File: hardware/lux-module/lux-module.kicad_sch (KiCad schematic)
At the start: 7 parts, among them J1 Conn_01x04, U1 TSL25911FN, U2 TPD3E001DRLR

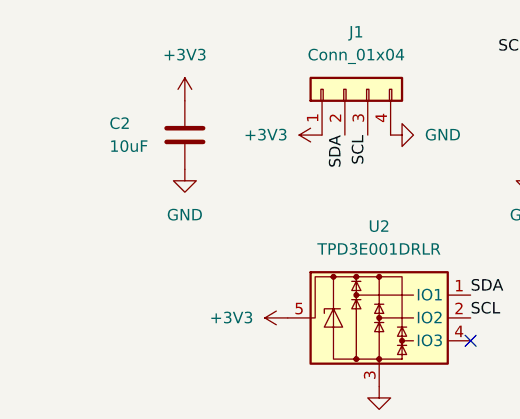
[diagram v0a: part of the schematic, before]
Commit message: review, add vias & ground pour
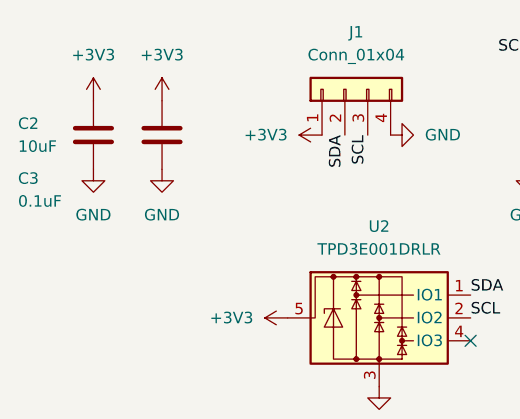
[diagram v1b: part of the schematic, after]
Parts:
- added C3: 0.1uF, Capacitor_SMD:C_0603_1608Metric, symbol Device:C
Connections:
- net +3V3: now also C3.1
- net GND: now also C3.2
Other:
- moved on the sheet: C2

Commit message: pad clearance & BOM fixes
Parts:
- C3: MPN GRM155R71H104KE14D -> CC0603KRX7R9BB104
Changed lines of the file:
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@@
 			)
 		)
-		(property "MPN" "GRM155R71H104KE14D"
+		(property "MPN" "CC0603KRX7R9BB104"
 			(at 82.55 96.52 0)
 			(effects

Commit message: swap connector in progress
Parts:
- J1: footprint 530480410:MOLEX_530480410 -> S04B_PASK_2:CONN4_S04B-PASK_JST
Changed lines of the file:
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@@
 			)
 		)
-		(property "Footprint" "530480410:MOLEX_530480410"
+		(property "Footprint" "S04B_PASK_2:CONN4_S04B-PASK_JST"
 			(at 102.87 91.44 0)
 			(effects

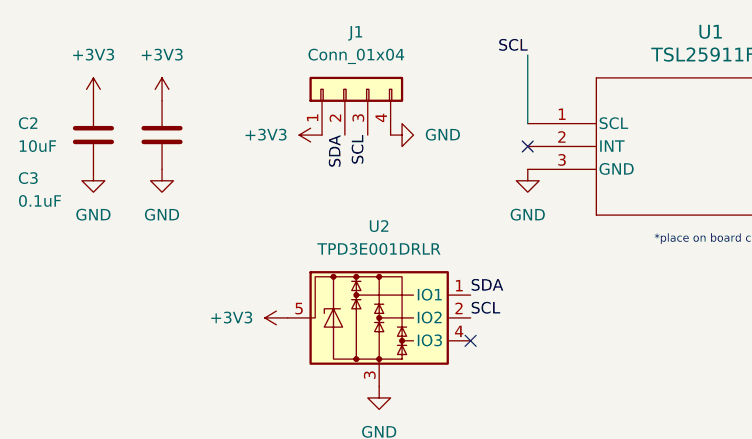
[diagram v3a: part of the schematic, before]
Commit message: connector fixes
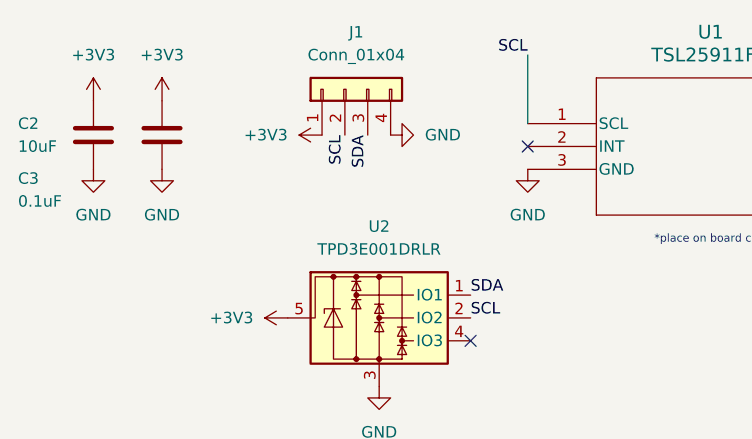
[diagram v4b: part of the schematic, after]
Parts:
- J1: MPN N/A -> S04B-PASK-2; Purchase No -> Yes
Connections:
- net SCL: now also J1.2 (Pin_2); no longer J1.3 (Pin_3)
- net SDA: now also J1.3 (Pin_3); no longer J1.2 (Pin_2)
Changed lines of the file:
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@@
 	)
 	(label "SDA"
-		(at 102.87 96.52 270)
+		(at 163.83 87.63 0)
 		(fields_autoplaced yes)
 		(effects
@@
 				(size 1.27 1.27)
 			)
-			(justify right bottom)
+			(justify left bottom)
 		)
 	)
 	(label "SDA"
-		(at 163.83 87.63 0)
+		(at 105.41 96.52 270)
 		(fields_autoplaced yes)
 		(effects
@@
 				(size 1.27 1.27)
 			)
-			(justify left bottom)
+			(justify right bottom)
 		)
 	)
 	(label "SCL"
-		(at 105.41 96.52 270)
+		(at 102.87 96.52 270)
 		(fields_autoplaced yes)
 		(effects
@@
 			)
 		)
-		(property "MPN" "N/A"
+		(property "MPN" "S04B-PASK-2"
 			(at 102.87 91.44 0)
 			(effects
@@
 			)
 		)
-		(property "Purchase" "No"
+		(property "Purchase" "Yes"
 			(at 102.87 91.44 0)
 			(effects

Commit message: work
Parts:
- C1: footprint Capacitor_SMD:C_0402_1005Metric -> Capacitor_SMD:C_0805_2012Metric; MPN CL05A105KP5NNNC -> C0805C104K5RACTU
- C2: footprint Capacitor_SMD:C_0603_1608Metric -> Capacitor_SMD:C_0805_2012Metric; MPN CL10A106KP8NNNC -> CL21B106KOQNNNE
- C3: footprint Capacitor_SMD:C_0603_1608Metric -> Capacitor_SMD:C_0805_2012Metric; MPN CC0603KRX7R9BB104 -> CL21B104KBCNNNC
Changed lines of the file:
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@@
 			)
 		)
-		(property "Footprint" "Capacitor_SMD:C_0603_1608Metric"
+		(property "Footprint" "Capacitor_SMD:C_0805_2012Metric"
 			(at 75.8952 100.33 0)
 			(effects
@@
 			)
 		)
-		(property "MPN" "CL10A106KP8NNNC"
+		(property "MPN" "CL21B106KOQNNNE"
 			(at 74.93 96.52 0)
 			(effects
@@
 			)
 		)
-		(property "Footprint" "Capacitor_SMD:C_0402_1005Metric"
+		(property "Footprint" "Capacitor_SMD:C_0805_2012Metric"
 			(at 172.4152 105.41 0)
 			(effects
@@
 			)
 		)
-		(property "MPN" "CL05A105KP5NNNC"
+		(property "MPN" "C0805C104K5RACTU"
 			(at 171.45 101.6 0)
 			(effects
@@
 			)
 		)
-		(property "Footprint" "Capacitor_SMD:C_0603_1608Metric"
+		(property "Footprint" "Capacitor_SMD:C_0805_2012Metric"
 			(at 83.5152 100.33 0)
 			(effects
@@
 			)
 		)
-		(property "MPN" "CC0603KRX7R9BB104"
+		(property "MPN" "CL21B104KBCNNNC"
 			(at 82.55 96.52 0)
 			(effects

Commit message: update ALS
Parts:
- added D1: LED, LED_SMD:LED_0603_1608Metric, symbol Device:LED
- added H3, H4: MountingHole, MountingHole:MountingHole_2.2mm_M2, symbol Mechanical:MountingHole
- added R1: 470, Resistor_SMD:R_0402_1005Metric, symbol Device:R
- C2: value 10uF -> 1uF
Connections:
- net +3V3: now also R1.2
- net GND: now also D1.1 (K)
- net SCL: now also U2.1 (IO1); no longer U2.2 (IO2)
- net SDA: now also U2.2 (IO2); no longer U2.1 (IO1)
- new net: D1.2 (A), R1.1
